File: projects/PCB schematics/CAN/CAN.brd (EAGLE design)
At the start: 99.1 x 99.1 mm, 11 parts

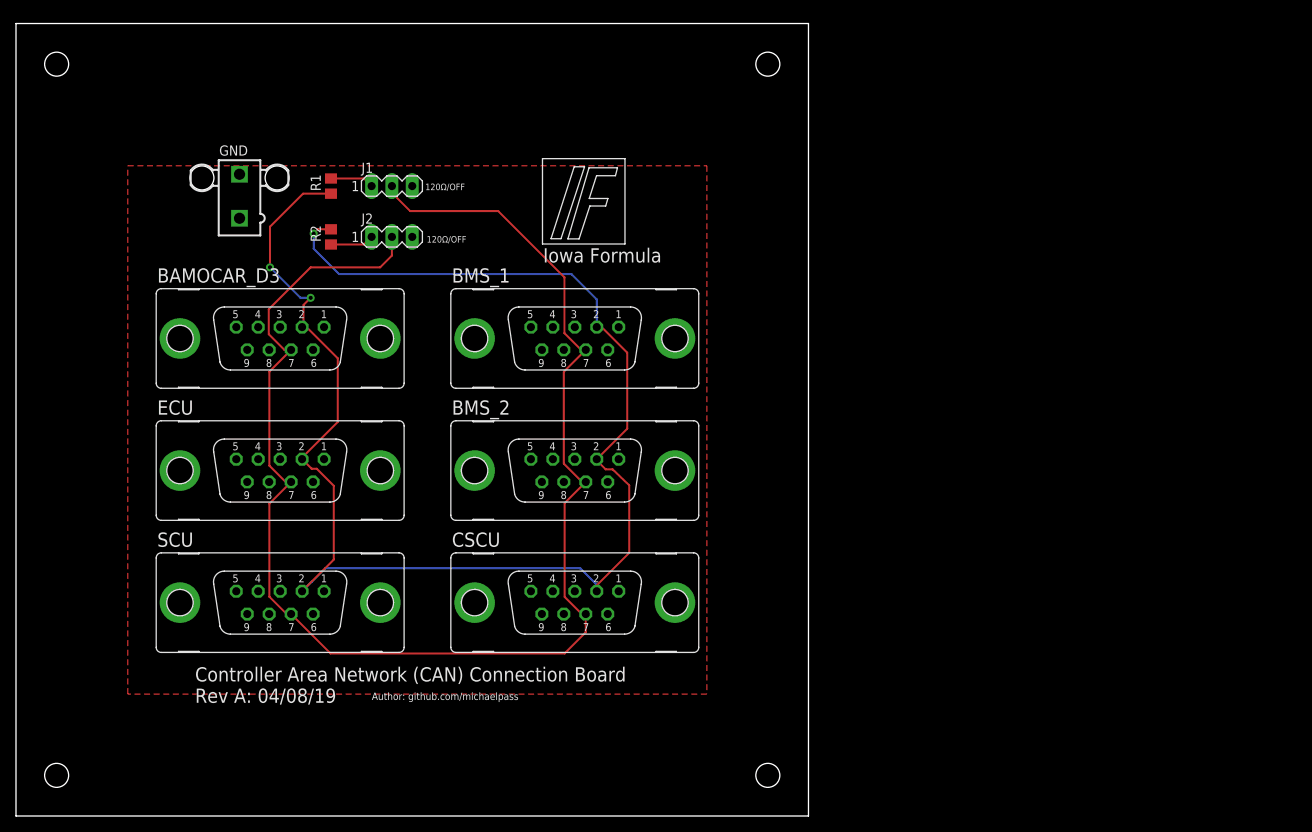
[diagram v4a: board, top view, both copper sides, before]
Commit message: PROJ - Silkscreen modifications - 50%.
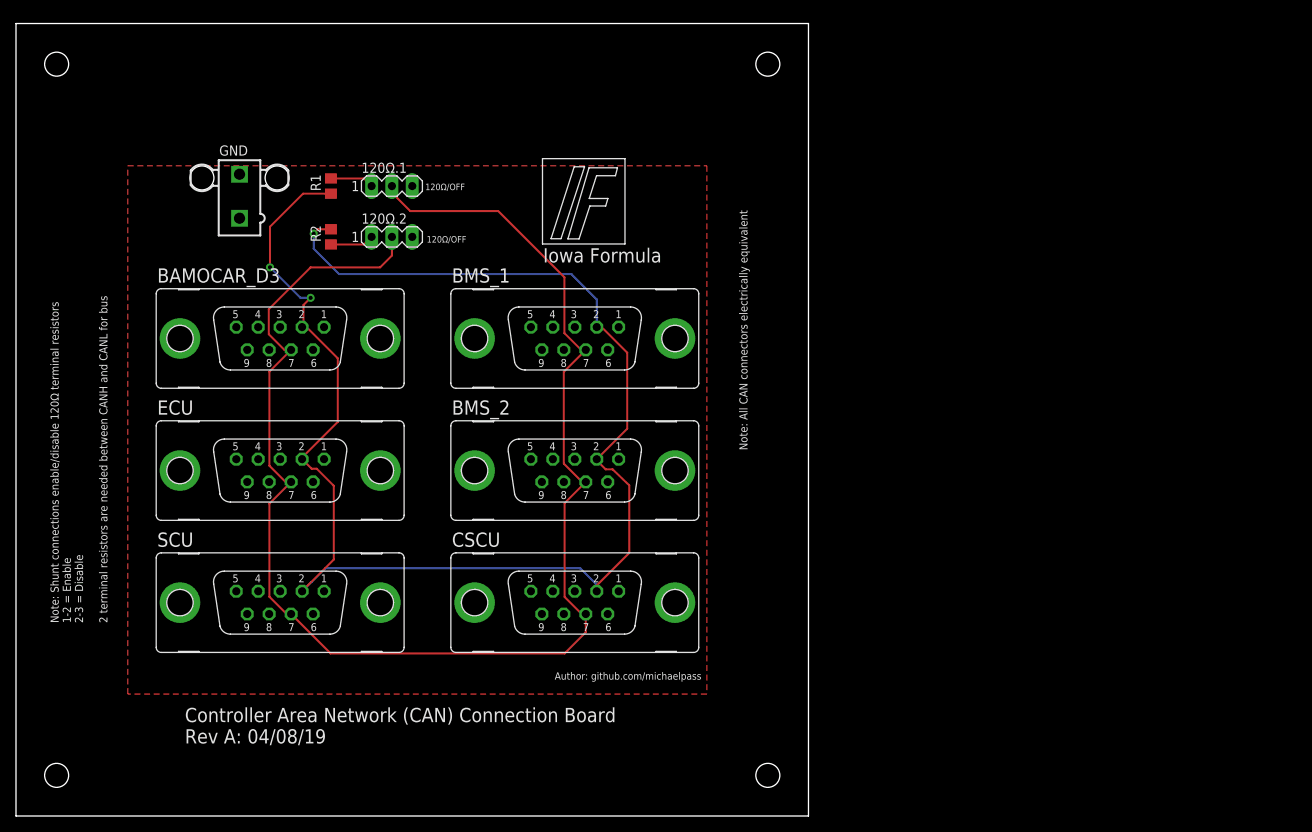
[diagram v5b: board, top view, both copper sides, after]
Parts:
- renumbered J1 to 120Ω.1, J2 to 120Ω.2
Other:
- board text added: "Note: All CAN connectors electrically equivalent"
- board text added: "Note: Shunt connections enable/disable 120Ω terminal resistors 1-2 = Enable 2-3 = Disable 2 terminal resistors are needed between CANH and CANL for bus"
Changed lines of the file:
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@@
 <wire x1="99.06" y1="99.06" x2="0" y2="99.06" width="0" layer="20"/>
 <wire x1="0" y1="99.06" x2="0" y2="0" width="0" layer="20"/>
-<text x="22.3774" y="14.1478" size="1.778" layer="25" font="vector">Controller Area Network (CAN) Connection Board
+<text x="21.1074" y="9.0678" size="1.778" layer="25" font="vector">Controller Area Network (CAN) Connection Board
 Rev A: 04/08/19</text>
-<text x="44.4754" y="14.5034" size="0.9144" layer="25">Author: github.com/michaelpass</text>
+<text x="67.3354" y="17.0434" size="0.9144" layer="25">Author: github.com/michaelpass</text>
 <wire x1="65.8114" y1="82.169" x2="65.8114" y2="71.501" width="0.1524" layer="25"/>
 <wire x1="65.8114" y1="71.501" x2="76.1238" y2="71.501" width="0.1524" layer="25"/>
@@
 <text x="51.3334" y="71.6788" size="0.8128" layer="25">120Ω/OFF</text>
 <text x="51.1556" y="78.232" size="0.8128" layer="25">120Ω/OFF</text>
+<text x="11.43" y="24.13" size="1.016" layer="21" rot="R90">Note: Shunt connections enable/disable 120Ω terminal resistors
+1-2 = Enable
+2-3 = Disable
+2 terminal resistors are needed between CANH and CANL for bus</text>
+<text x="91.44" y="45.72" size="1.016" layer="21" rot="R90">Note: All CAN connectors electrically equivalent</text>
 </plain>
 <attributes>
@@
 <attribute name="OC_NEWARK" value="unknown" x="27.94" y="77.47" size="1.778" layer="27" display="off"/>
 </element>
-<element name="J1" library="con-lstb" library_urn="urn:adsk.eagle:library:162" package="MA03-1" package3d_urn="urn:adsk.eagle:package:8339/1" value="" x="46.99" y="78.74" smashed="yes">
+<element name="120Ω.1" library="con-lstb" library_urn="urn:adsk.eagle:library:162" package="MA03-1" package3d_urn="urn:adsk.eagle:package:8339/1" value="" x="46.99" y="78.74" smashed="yes">
 <attribute name="MF" value="" x="46.99" y="78.74" size="1.778" layer="27" display="off"/>
 <attribute name="MPN" value="" x="46.99" y="78.74" size="1.778" layer="27" display="off"/>
@@
 <attribute name="VALUE" x="43.18" y="75.819" size="1.27" layer="27" ratio="10"/>
 </element>
-<element name="J2" library="con-lstb" library_urn="urn:adsk.eagle:library:162" package="MA03-1" package3d_urn="urn:adsk.eagle:package:8339/1" value="" x="46.99" y="72.39" smashed="yes">
+<element name="120Ω.2" library="con-lstb" library_urn="urn:adsk.eagle:library:162" package="MA03-1" package3d_urn="urn:adsk.eagle:package:8339/1" value="" x="46.99" y="72.39" smashed="yes">
 <attribute name="MF" value="" x="46.99" y="72.39" size="1.778" layer="27" display="off"/>
 <attribute name="MPN" value="" x="46.99" y="72.39" size="1.778" layer="27" display="off"/>
@@
 <attribute name="NAME" x="38.1" y="78.105" size="1.27" layer="25" rot="R90"/>
 <attribute name="SPICEPREFIX" value="R" x="39.37" y="78.74" size="1.778" layer="27" rot="R270" display="off"/>
-<attribute name="VALUE" x="36.83" y="79.375" size="1.27" layer="27" rot="R270"/>
 </element>
 <element name="R2" library="rcl" library_urn="urn:adsk.eagle:library:334" package="R0805" package3d_urn="urn:adsk.eagle:package:23553/2" value="120" x="39.37" y="72.39" smashed="yes" rot="R90">
 <attribute name="NAME" x="38.1" y="71.755" size="1.27" layer="25" rot="R90"/>
 <attribute name="SPICEPREFIX" value="R" x="39.37" y="72.39" size="1.778" layer="27" rot="R90" display="off"/>
-<attribute name="VALUE" x="41.91" y="71.755" size="1.27" layer="27" rot="R90"/>
 </element>
 </elements>
@@
 </signal>
 <signal name="N$2">
-<contactref element="J2" pad="3"/>
+<contactref element="120Ω.2" pad="3"/>
 </signal>
 <signal name="N$3">
 <contactref element="R2" pad="1"/>
-<contactref element="J2" pad="1"/>
+<contactref element="120Ω.2" pad="1"/>
 <wire x1="39.37" y1="71.44" x2="43.5" y2="71.44" width="0.254" layer="1"/>
 <wire x1="43.5" y1="71.44" x2="44.45" y2="72.39" width="0.254" layer="1"/>
@@
 <signal name="N$4">
 <contactref element="R1" pad="1"/>
-<contactref element="J1" pad="1"/>
+<contactref element="120Ω.1" pad="1"/>
 <wire x1="39.37" y1="79.69" x2="43.5" y2="79.69" width="0.254" layer="1"/>
 <wire x1="43.5" y1="79.69" x2="44.45" y2="78.74" width="0.254" layer="1"/>
@@
 </signal>
 <signal name="N$6">
-<contactref element="J1" pad="3"/>
+<contactref element="120Ω.1" pad="3"/>
 </signal>
 <signal name="CANH">
-<contactref element="J2" pad="2"/>
-<contactref element="J1" pad="2"/>
+<contactref element="120Ω.2" pad="2"/>
+<contactref element="120Ω.1" pad="2"/>
 <contactref element="BMS_1" pad="7"/>
 <contactref element="BMS_2" pad="7"/>

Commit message: PROJ - Gerber files major milestone - 05/05/19.
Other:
- board text added: "Controller Area Network (CAN) Connection Board Rev A: 05/05/19"
- board text removed: "Controller Area Network (CAN) Connection Board Rev A: 04/08/19"
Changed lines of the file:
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@@
 <wire x1="0" y1="99.06" x2="0" y2="0" width="0" layer="20"/>
 <text x="21.1074" y="9.0678" size="1.778" layer="25" font="vector">Controller Area Network (CAN) Connection Board
-Rev A: 04/08/19</text>
+Rev A: 05/05/19</text>
 <text x="67.3354" y="17.0434" size="0.9144" layer="25">Author: github.com/michaelpass</text>
 <wire x1="65.8114" y1="82.169" x2="65.8114" y2="71.501" width="0.1524" layer="25"/>
